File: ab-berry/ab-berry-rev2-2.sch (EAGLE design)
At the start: 74 parts, among them IC1 STM32F303CCT6, IC2 AT45DB161D-SU, Q1 BSS84, U1 LM1117MPX-3.3/NOPB or AP2114H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, U2 PRTR5V0U2X, X1 04-JST-B4B-XH-A, X2 04-JST-B4B-XH-A, X3 ABM7-8.000MHZ-D2Y-T

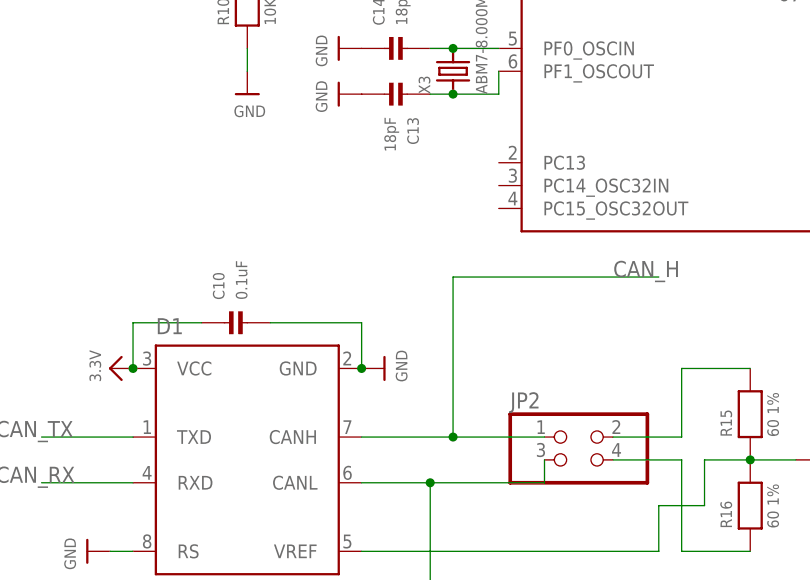
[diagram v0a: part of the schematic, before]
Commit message: ab-berry: master jumper, phi branding, some macrofab attribs
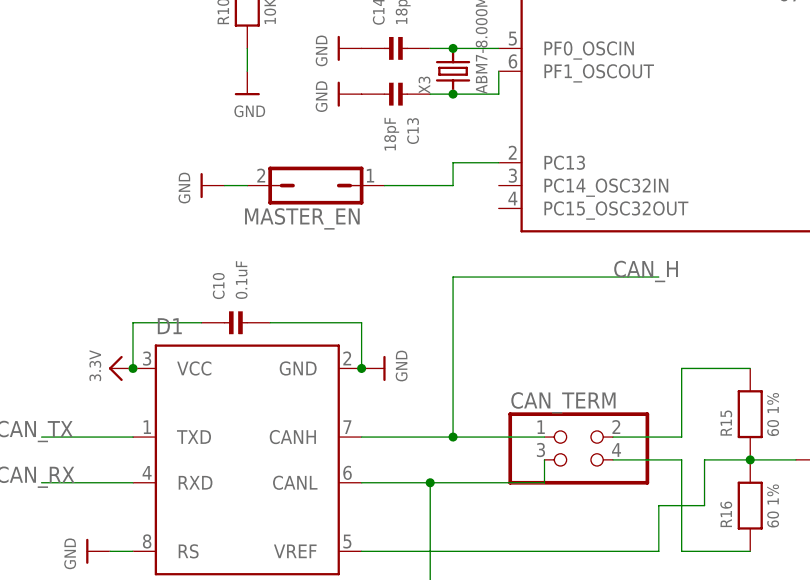
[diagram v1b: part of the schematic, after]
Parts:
- added MASTER_EN: (no value), jumper:JP1Q
- renumbered JP2 to CAN_TERM
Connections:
- new net N$22: IC1.PC13, MASTER_EN.1
- net GND: now also MASTER_EN.2
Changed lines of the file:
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@@
 <part name="X2" library="bt_con-jst-xh" deviceset="04-JST" device="-B4B-XH-A"/>
 <part name="X1" library="bt_con-jst-xh" deviceset="04-JST" device="-B4B-XH-A"/>
-<part name="JP2" library="pinhead" deviceset="PINHD-2X2" device=""/>
+<part name="CAN_TERM" library="pinhead" deviceset="PINHD-2X2" device=""/>
 <part name="Q1" library="transistor-small-signal" deviceset="BSS84" device=""/>
 <part name="R22" library="microbuilder" deviceset="RESISTOR" device="0603" value="1.5k"/>
 <part name="3.3V16" library="microbuilder" deviceset="3.3V" device=""/>
+<part name="MASTER_EN" library="jumper" deviceset="JP1Q" device=""/>
+<part name="GND41" library="microbuilder" deviceset="GND" device=""/>
 </parts>
 <sheets>
@@
 <instance part="X1" gate="-3" x="-71.12" y="38.1"/>
 <instance part="X1" gate="-4" x="-71.12" y="35.56"/>
-<instance part="JP2" gate="A" x="33.02" y="-25.4"/>
+<instance part="CAN_TERM" gate="A" x="33.02" y="-25.4"/>
 <instance part="Q1" gate="G$1" x="114.3" y="88.9" rot="MR180"/>
 <instance part="R22" gate="G$1" x="114.3" y="101.6" rot="R270"/>
 <instance part="3.3V16" gate="G$1" x="114.3" y="78.74" rot="R180"/>
+<instance part="MASTER_EN" gate="A" x="2.54" y="5.08" rot="R90"/>
+<instance part="GND41" gate="G$1" x="-10.16" y="5.08" rot="R270"/>
 </instances>
 <busses>
@@
 <wire x1="-20.32" y1="-35.56" x2="-17.78" y2="-35.56" width="0.1524" layer="91"/>
 <pinref part="GND12" gate="G$1" pin="GND"/>
+</segment>
+<segment>
+<pinref part="MASTER_EN" gate="A" pin="2"/>
+<pinref part="GND41" gate="G$1" pin="GND"/>
+<wire x1="-7.62" y1="5.08" x2="-5.08" y2="5.08" width="0.1524" layer="91"/>
 </segment>
 </net>
@@
 <wire x1="17.78" y1="-5.08" x2="40.64" y2="-5.08" width="0.1524" layer="91"/>
 <label x="35.56" y="-5.08" size="1.778" layer="95"/>
-<pinref part="JP2" gate="A" pin="1"/>
+<pinref part="CAN_TERM" gate="A" pin="1"/>
 <wire x1="27.94" y1="-22.86" x2="17.78" y2="-22.86" width="0.1524" layer="91"/>
 <junction x="17.78" y="-22.86"/>
@@
 <label x="35.56" y="-43.18" size="1.778" layer="95"/>
 <wire x1="15.24" y1="-43.18" x2="43.18" y2="-43.18" width="0.1524" layer="91"/>
-<pinref part="JP2" gate="A" pin="3"/>
+<pinref part="CAN_TERM" gate="A" pin="3"/>
 <wire x1="15.24" y1="-27.94" x2="27.94" y2="-27.94" width="0.1524" layer="91"/>
 <wire x1="27.94" y1="-27.94" x2="27.94" y2="-25.4" width="0.1524" layer="91"/>
@@
 <net name="N$4" class="0">
 <segment>
-<pinref part="JP2" gate="A" pin="2"/>
+<pinref part="CAN_TERM" gate="A" pin="2"/>
 <wire x1="35.56" y1="-22.86" x2="43.18" y2="-22.86" width="0.1524" layer="91"/>
 <wire x1="43.18" y1="-22.86" x2="43.18" y2="-15.24" width="0.1524" layer="91"/>
@@
 <net name="N$5" class="0">
 <segment>
-<pinref part="JP2" gate="A" pin="4"/>
+<pinref part="CAN_TERM" gate="A" pin="4"/>
 <wire x1="35.56" y1="-25.4" x2="43.18" y2="-25.4" width="0.1524" layer="91"/>
 <wire x1="43.18" y1="-25.4" x2="43.18" y2="-35.56" width="0.1524" layer="91"/>
@@
 </segment>
 </net>
+<net name="N$22" class="0">
+<segment>
+<pinref part="IC1" gate="G$1" pin="PC13"/>
+<wire x1="22.86" y1="7.62" x2="17.78" y2="7.62" width="0.1524" layer="91"/>
+<wire x1="17.78" y1="7.62" x2="17.78" y2="5.08" width="0.1524" layer="91"/>
+<wire x1="17.78" y1="5.08" x2="10.16" y2="5.08" width="0.1524" layer="91"/>
+<pinref part="MASTER_EN" gate="A" pin="1"/>
+</segment>
+</net>

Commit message: ab-berry rev2-2 sent to macrofab
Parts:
- C15: MPN (none) -> CL10A475MP5LNNC
- IC2, JP1, X4: POPULATE (none) -> 0
- Q1: MPN (none) -> BSS84
- R15, R16: MPN (none) -> MF-RES-0603-60.4
- R21, R9: MPN (none) -> MF-RES-0603-330
- R22: MPN (none) -> MCR03ERTF1501
- R23, R24: MPN (none) -> MF-RES-0603-22
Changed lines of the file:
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@@
 <part name="C9" library="microbuilder" deviceset="CAP_CERAMIC" device="0603" value="0.01uF"/>
 <part name="C8" library="microbuilder" deviceset="CAP_CERAMIC" device="0603" value="1uF"/>
-<part name="C15" library="microbuilder" deviceset="CAP_CERAMIC" device="0603" value="4.7uF"/>
+<part name="C15" library="microbuilder" deviceset="CAP_CERAMIC" device="0603" value="4.7uF">
+<attribute name="MPN" value="CL10A475MP5LNNC"/>
+</part>
 <part name="GND17" library="microbuilder" deviceset="GND" device=""/>
 <part name="TC1" library="TagConnect" deviceset="TC2050-IDC" device="-NL"/>
@@
 <part name="3.3V6" library="microbuilder" deviceset="3.3V" device=""/>
 <part name="LED1" library="microbuilder" deviceset="LED" device="0603"/>
-<part name="R9" library="microbuilder" deviceset="RESISTOR" device="0603" value="330"/>
+<part name="R9" library="microbuilder" deviceset="RESISTOR" device="0603" value="330">
+<attribute name="MPN" value="MF-RES-0603-330"/>
+</part>
 <part name="GND11" library="microbuilder" deviceset="GND" device=""/>
 <part name="ROT2" library="keves" deviceset="PEC11-4215K-S0024" device="" value="PEC12R-4225F-S0024"/>
@@
 <part name="H4" library="holes" deviceset="MOUNT-HOLE" device="3.2" value="MOUNT-HOLE3.2"/>
 <part name="5.0V1" library="microbuilder" deviceset="5.0V" device=""/>
-<part name="JP1" library="pinhead" deviceset="PINHD-1X2" device=""/>
+<part name="JP1" library="pinhead" deviceset="PINHD-1X2" device="">
+<attribute name="POPULATE" value="0"/>
+</part>
 <part name="3.3V3" library="microbuilder" deviceset="3.3V" device=""/>
 <part name="GND7" library="microbuilder" deviceset="GND" device=""/>
-<part name="R21" library="microbuilder" deviceset="RESISTOR" device="0603" value="330"/>
+<part name="R21" library="microbuilder" deviceset="RESISTOR" device="0603" value="330">
+<attribute name="MPN" value="MF-RES-0603-330"/>
+</part>
 <part name="LED2" library="microbuilder" deviceset="LED" device="0603"/>
 <part name="GND34" library="microbuilder" deviceset="GND" device=""/>
@@
 <part name="C5" library="SparkFun-Capacitors" deviceset="10UF-6.3V-20%(0603)(TANT)" device="&quot;" value="10uF TANT"/>
 <part name="IC1" library="keves" deviceset="STM32F302_F303_B_C_LQFP48" device="" value="STM32F303CCT6"/>
-<part name="X4" library="keves" deviceset="TE-292304-1" device=""/>
-<part name="R24" library="microbuilder" deviceset="RESISTOR" device="0603" value="22"/>
-<part name="R23" library="microbuilder" deviceset="RESISTOR" device="0603" value="22"/>
+<part name="X4" library="keves" deviceset="TE-292304-1" device="">
+<attribute name="POPULATE" value="0"/>
+</part>
+<part name="R24" library="microbuilder" deviceset="RESISTOR" device="0603" value="22">
+<attribute name="MPN" value="MF-RES-0603-22"/>
+</part>
+<part name="R23" library="microbuilder" deviceset="RESISTOR" device="0603" value="22">
+<attribute name="MPN" value="MF-RES-0603-22"/>
+</part>
 <part name="5.0V4" library="microbuilder" deviceset="5.0V" device=""/>
 <part name="GND37" library="microbuilder" deviceset="GND" device=""/>
@@
 <part name="GND33" library="microbuilder" deviceset="GND" device=""/>
 <part name="5.0V3" library="microbuilder" deviceset="5.0V" device=""/>
-<part name="IC2" library="atmel" deviceset="AT45DB161D" device="-SU"/>
+<part name="IC2" library="atmel" deviceset="AT45DB161D" device="-SU">
+<attribute name="POPULATE" value="0"/>
+</part>
 <part name="C23" library="microbuilder" deviceset="CAP_CERAMIC" device="0603" value="0.1uF"/>
 <part name="GND39" library="microbuilder" deviceset="GND" device=""/>
@@
 <part name="3.3V18" library="microbuilder" deviceset="3.3V" device=""/>
 <part name="3.3V17" library="microbuilder" deviceset="3.3V" device=""/>
-<part name="R16" library="microbuilder" deviceset="RESISTOR" device="0603" value="60 1%"/>
-<part name="R15" library="microbuilder" deviceset="RESISTOR" device="0603" value="60 1%"/>
+<part name="R16" library="microbuilder" deviceset="RESISTOR" device="0603" value="60 1%">
+<attribute name="MPN" value="MF-RES-0603-60.4"/>
+</part>
+<part name="R15" library="microbuilder" deviceset="RESISTOR" device="0603" value="60 1%">
+<attribute name="MPN" value="MF-RES-0603-60.4"/>
+</part>
 <part name="C19" library="microbuilder" deviceset="CAP_CERAMIC" device="0603" value="4.7nF"/>
 <part name="GND27" library="microbuilder" deviceset="GND" device=""/>
@@
 <part name="X1" library="bt_con-jst-xh" deviceset="04-JST" device="-B4B-XH-A"/>
 <part name="CAN_TERM" library="pinhead" deviceset="PINHD-2X2" device=""/>
-<part name="Q1" library="transistor-small-signal" deviceset="BSS84" device=""/>
-<part name="R22" library="microbuilder" deviceset="RESISTOR" device="0603" value="1.5k"/>
+<part name="Q1" library="transistor-small-signal" deviceset="BSS84" device="">
+<attribute name="MPN" value="BSS84"/>
+</part>
+<part name="R22" library="microbuilder" deviceset="RESISTOR" device="0603" value="1.5k">
+<attribute name="MPN" value="MCR03ERTF1501"/>
+</part>
 <part name="3.3V16" library="microbuilder" deviceset="3.3V" device=""/>
 <part name="MASTER_EN" library="jumper" deviceset="JP1Q" device=""/>
@@
 <instance part="C9" gate="G$1" x="-5.08" y="71.12" rot="R90"/>
 <instance part="C8" gate="G$1" x="-7.62" y="66.04" rot="R270"/>
-<instance part="C15" gate="G$1" x="17.78" y="86.36" rot="R90"/>
+<instance part="C15" gate="G$1" x="17.78" y="86.36" rot="R90">
+<attribute name="MPN" x="17.78" y="86.36" size="1.778" layer="96" rot="R90" display="off"/>
+</instance>
 <instance part="GND17" gate="G$1" x="-12.7" y="93.98" rot="R180"/>
 <instance part="TC1" gate="A" x="-10.16" y="38.1" rot="R180"/>
@@
 <instance part="3.3V6" gate="G$1" x="-33.02" y="83.82" rot="R270"/>
 <instance part="LED1" gate="G$1" x="-38.1" y="63.5" rot="R270"/>
-<instance part="R9" gate="G$1" x="-38.1" y="76.2" rot="R90"/>
+<instance part="R9" gate="G$1" x="-38.1" y="76.2" rot="R90">
+<attribute name="MPN" x="-38.1" y="76.2" size="1.778" layer="96" rot="R90" display="off"/>
+</instance>
 <instance part="GND11" gate="G$1" x="-38.1" y="55.88"/>
 <instance part="ROT2" gate="G$1" x="-58.42" y="116.84" rot="R270"/>
@@
 <instance part="H4" gate="G$1" x="-63.5" y="93.98"/>
 <instance part="5.0V1" gate="G$1" x="-83.82" y="43.18" rot="R90"/>
-<instance part="JP1" gate="G$1" x="-66.04" y="55.88"/>
+<instance part="JP1" gate="G$1" x="-66.04" y="55.88">
+<attribute name="POPULATE" x="-66.04" y="55.88" size="1.778" layer="96" display="off"/>
+</instance>
 <instance part="3.3V3" gate="G$1" x="-71.12" y="58.42" rot="R90"/>
 <instance part="GND7" gate="G$1" x="-71.12" y="55.88" rot="R270"/>
-<instance part="R21" gate="G$1" x="106.68" y="48.26" rot="R180"/>
+<instance part="R21" gate="G$1" x="106.68" y="48.26" rot="R180">
+<attribute name="MPN" x="106.68" y="48.26" size="1.778" layer="96" rot="R180" display="off"/>
+</instance>
 <instance part="LED2" gate="G$1" x="119.38" y="48.26"/>
 <instance part="GND34" gate="G$1" x="127" y="48.26" rot="R90"/>
@@
 <instance part="IC1" gate="G$1" x="53.34" y="58.42"/>
 <instance part="X4" gate="_CONN" x="154.94" y="109.22"/>
-<instance part="X4" gate="SHIELD" x="154.94" y="111.76"/>
-<instance part="R24" gate="G$1" x="137.16" y="111.76" rot="R180"/>
-<instance part="R23" gate="G$1" x="124.46" y="109.22" rot="R180"/>
+<instance part="X4" gate="SHIELD" x="154.94" y="111.76">
+<attribute name="POPULATE" x="154.94" y="111.76" size="1.778" layer="96" display="off"/>
+</instance>
+<instance part="R24" gate="G$1" x="137.16" y="111.76" rot="R180">
+<attribute name="MPN" x="137.16" y="111.76" size="1.778" layer="96" rot="R180" display="off"/>
+</instance>
+<instance part="R23" gate="G$1" x="124.46" y="109.22" rot="R180">
+<attribute name="MPN" x="124.46" y="109.22" size="1.778" layer="96" rot="R180" display="off"/>
+</instance>
 <instance part="5.0V4" gate="G$1" x="152.4" y="124.46"/>
 <instance part="GND37" gate="G$1" x="152.4" y="99.06"/>
@@
 <instance part="GND33" gate="G$1" x="127" y="149.86" rot="R180"/>
 <instance part="5.0V3" gate="G$1" x="127" y="119.38" rot="R180"/>
-<instance part="IC2" gate="G$1" x="147.32" y="15.24"/>
+<instance part="IC2" gate="G$1" x="147.32" y="15.24">
+<attribute name="POPULATE" x="147.32" y="15.24" size="1.778" layer="96" display="off"/>
+</instance>
 <instance part="C23" gate="G$1" x="160.02" y="30.48" rot="R180"/>
 <instance part="GND39" gate="G$1" x="160.02" y="38.1" rot="R180"/>
@@
 <instance part="3.3V18" gate="G$1" x="116.84" y="15.24" rot="R90"/>
 <instance part="3.3V17" gate="G$1" x="116.84" y="20.32" rot="R90"/>
-<instance part="R16" gate="G$1" x="50.8" y="-30.48" rot="R90"/>
-<instance part="R15" gate="G$1" x="50.8" y="-20.32" rot="R90"/>
+<instance part="R16" gate="G$1" x="50.8" y="-30.48" rot="R90">
+<attribute name="MPN" x="50.8" y="-30.48" size="1.778" layer="96" rot="R90" display="off"/>
+</instance>
+<instance part="R15" gate="G$1" x="50.8" y="-20.32" rot="R90">
+<attribute name="MPN" x="50.8" y="-20.32" size="1.778" layer="96" rot="R90" display="off"/>
+</instance>
 <instance part="C19" gate="G$1" x="58.42" y="-25.4" rot="R270"/>
 <instance part="GND27" gate="G$1" x="68.58" y="-25.4" rot="R90"/>
@@
 <instance part="X1" gate="-4" x="-71.12" y="35.56"/>
 <instance part="CAN_TERM" gate="A" x="33.02" y="-25.4"/>
-<instance part="Q1" gate="G$1" x="114.3" y="88.9" rot="MR180"/>
-<instance part="R22" gate="G$1" x="114.3" y="101.6" rot="R270"/>
+<instance part="Q1" gate="G$1" x="114.3" y="88.9" rot="MR180">
+<attribute name="MPN" x="114.3" y="88.9" size="1.778" layer="96" rot="MR180" display="off"/>
+</instance>
+<instance part="R22" gate="G$1" x="114.3" y="101.6" rot="R270">
+<attribute name="MPN" x="114.3" y="101.6" size="1.778" layer="96" rot="R270" display="off"/>
+</instance>
 <instance part="3.3V16" gate="G$1" x="114.3" y="78.74" rot="R180"/>
 <instance part="MASTER_EN" gate="A" x="2.54" y="5.08" rot="R90"/>
